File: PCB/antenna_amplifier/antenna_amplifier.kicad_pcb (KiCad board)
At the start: 4 copper layers, 200 x 100 mm, 134 parts, among them J101 PWR_IN 9V, J201 FILT_IN, J202 BIAS, J401 AES3 OUT, J402 S/PDIF OUT, SW301 RESET, SW302 PCM1804 MODE, SW401 CS8406 MODE, U101 ADM7150ARDZ-5.0, U102 ADM7150ARDZ-3.3, U201 LMP7721, U202 LMP7715, U203 LMP7715, U301 LMP7715, U302 PCM1804, U401 CS8406, Y401 24.576MHz, Y402 24.576MHz

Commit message: Amplifier: decouplers next to their supply pins
C206 (U202), C304 (U301), C403 and C404 (U401, CS8406) were 6-8 mm from
the supply pins they decouple; now about 2 mm each. Re-routed; DRC: only
the intended island mask bridges, unconnected 0, parity 0; fit check
clean; fab package refreshed.

Co-Authored-By: Claude Opus 5.5 <noreply@anthropic.com>
Claude-Session: https://claude.ai/code/session_01RsM1DhHhY1tSr2aHjVygSC
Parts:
- moved C304 7.24 mm to (150.2, 64.0), turned to -90 degrees
- moved C404 7.01 mm to (214.4, 101.0), turned to 180 degrees
- moved C206 6.75 mm to (89.6, 115.0), turned to -90 degrees
- moved C403 6.21 mm to (225.6, 100.7), turned to 0 degrees
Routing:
- net /Clock and S/PDIF + AES3 output/APMS: track 80.8 -> 61.0 mm, vias 1 -> 2
- net /Clock and S/PDIF + AES3 output/HWCK1: track 85.8 -> 69.0 mm, vias 1 -> 0
- net /Clock and S/PDIF + AES3 output/CEN: track 62.1 -> 78.6 mm, vias 2 -> 1
- net /Clock and S/PDIF + AES3 output/EMPH_N: track 54.7 -> 70.4 mm, vias 0 -> 1
- net +5VA: track 106.5 -> 97.4 mm, vias 3 -> 4
- net +9V: track 101.0 -> 109.2 mm
- net +3V3: track 191.6 -> 185.0 mm, vias 1 -> 2
- net /ADC (PCM1804)/DRV_OUT: track 55.5 -> 61.3 mm, vias 3 -> 2
- net /Electrometer front end/BIAS_DIV: track 25.1 -> 30.5 mm
- net RESET_N: track 61.4 -> 66.5 mm, vias 3 -> 0
- net /ADC (PCM1804)/VCOML: track 84.3 -> 88.7 mm
- net /Clock and S/PDIF + AES3 output/SFMT1: track 62.9 -> 60.0 mm, vias 0 -> 2
- net /Clock and S/PDIF + AES3 output/HWCK0: track 95.3 -> 92.4 mm
- net GND: track 125.4 -> 127.2 mm, vias 748 -> 756
- net /ADC (PCM1804)/BYPAS: track 30.2 -> 28.4 mm
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
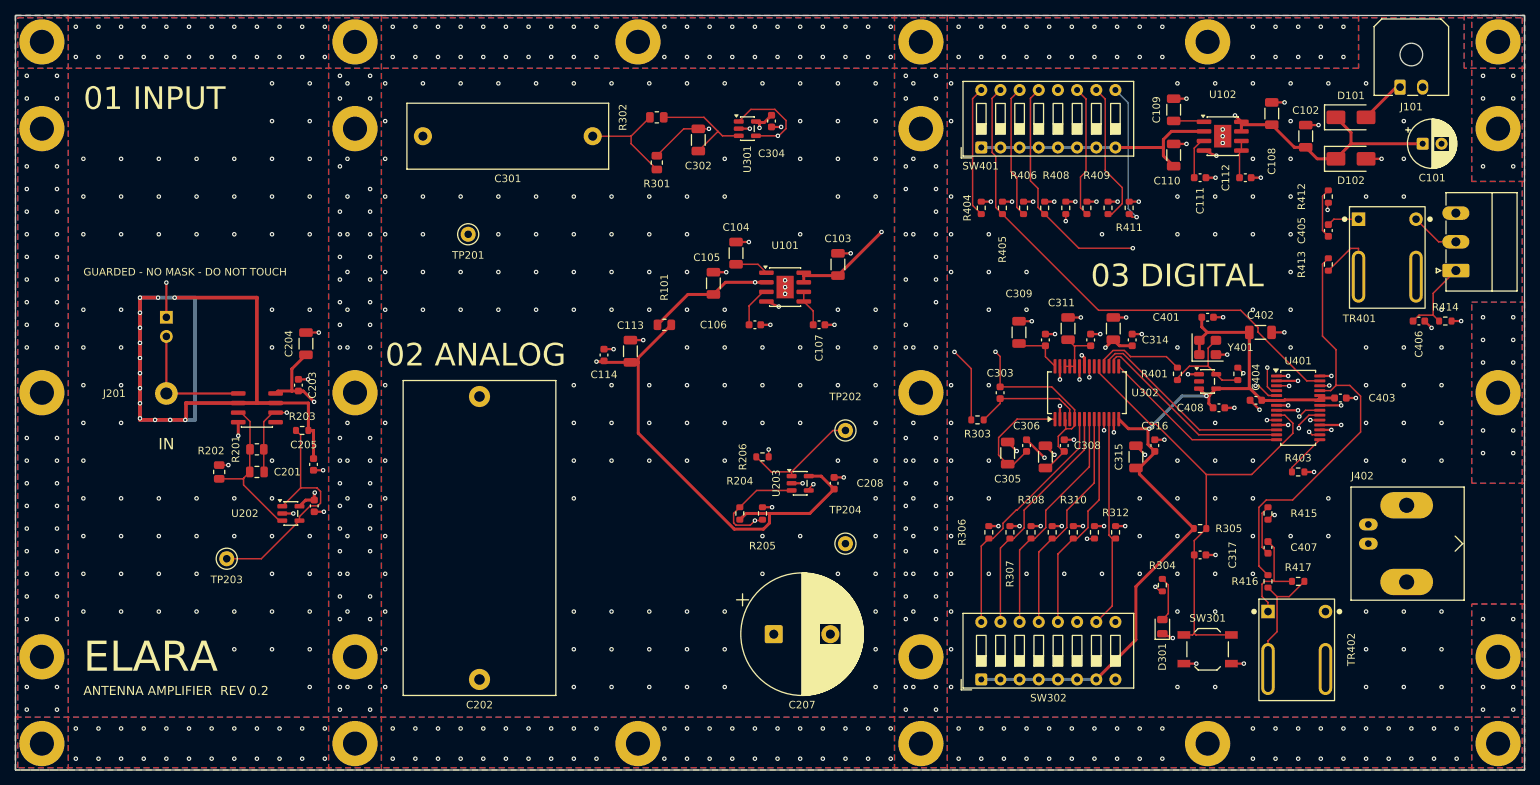
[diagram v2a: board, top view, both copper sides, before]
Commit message: Battery-friendly amplifier, RJ45 AES3 output, tidy placement, 1 mm PSU barrier
Amplifier schematic:
- No LEDs (battery use): the D301 overflow LED becomes test point TP301.
- PCM1804 FMT/S-M/OSR pins use the chip's internal 51 k pull-downs (6 resistors
  gone); BYPAS and the CS8406 mode pins get 47 k: about 3 mA less on +3V3.
- One output: AES3 on a shielded RJ45 (Amphenol RJHSE-5380, blue pair 4/5) for
  shielded twisted-pair cable, transformer isolated; the cable shield floats at
  the receiver (10 nF RF bond DNP, the DC bond is gone). The S/PDIF coax branch
  (BNC, second S22083, 5.6 mA standing current) is removed.

Layout:
- Amplifier re-placed in functional blocks on a 0.5 mm grid: PCM1804 and CS8406
  side by side so the I2S lines run straight, capacitor cells round the LDOs,
  DIP pull-downs in line with the switch pins, guard column in signal order with
  a re-routed hand guard-drive link. RJ45 notch 20 x 16 mm, BNC notch gone.
- PSU tidied (aligned columns, flyback diodes over their relays) and the charger
  / receiver copper kept >= 1.0 mm apart (was 0.30 mm): custom DRC rule, 1 mm
  router class for the relay contacts, hand-routed GND / GND_C at the relays.
- Reference labels follow each part's row; every label on silk except on the
  bare guard island. Fixed two placer bugs: each label counted as its own
  obstacle (SWIG proxies compared with 'is'), and unplaced labels blocked their
  neighbours. Texts are measured by their strokes, not KiCad's text cell.

Mechanics: RJ45 notch, plug envelope and a 1 mm isolation gap in fit_check.
BOM: 502 EUR as designed, 407 EUR recommended; 81 order lines.
Docs: STATUS, PLAN, ASSEMBLY, MOUNTING, README, mechanical and BOM notes;
MAINS_CABLE gains a certified DIY screened-cable option (H07RN-F + foil + braid)
and says why Ethernet cable must not carry mains.

All checks pass (tools/check_all.sh): ERC 0, DRC/parity 0 on all boards (only
the intended guard-island mask bridges), mains clearances, fit check, 27 tests.

Co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
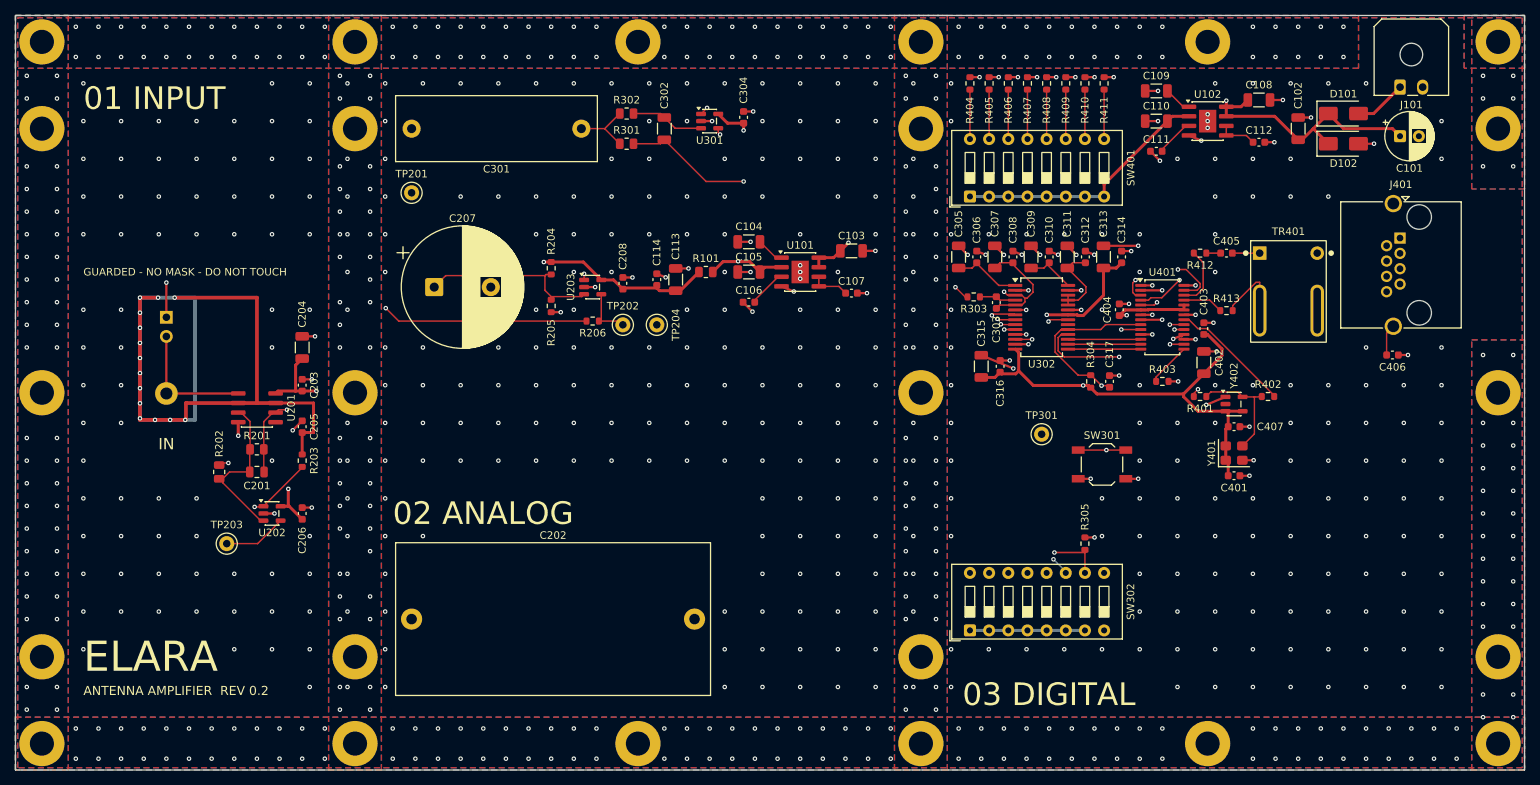
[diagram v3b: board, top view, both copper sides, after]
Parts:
- removed C408: 100n, Capacitor_SMD:C_0603_1608Metric
- removed D301: RED, LED_SMD:LED_0805_2012Metric
- removed J402: S/PDIF OUT, Connector_Coaxial:BNC_Amphenol_B6252HB-NPP3G-50_Horizontal
- removed R306, R307, R308, R309, R310, R311, R312: 10k, Resistor_SMD:R_0603_1608Metric
- removed R414: 0, Resistor_SMD:R_0603_1608Metric
- removed R415, R416: 249, Resistor_SMD:R_0603_1608Metric
- removed R417: 90.9, Resistor_SMD:R_0603_1608Metric
- removed TR402: S22083, elara:Transformer_Pulse_4Pin_W7.62mm
- added TP301: OVFL, TestPoint:TestPoint_Keystone_5000-5004_Miniature, F.Cu at (186.0, 105.5)
- J401: footprint Connector_Phoenix_MC:PhoenixContact_MC_1,5_3-G-3.81_1x03_P3.81mm_Horizontal -> Connector_RJ:RJ45_Amphenol_RJHSE5380
- R304: value 1k -> 10k
- R305, R403, R404, R405, R406, R407, R408, R409, R410, R411: value 10k -> 47k
- moved C207 64.4 mm to (105.5, 86.0)
- moved R204 41.0 mm to (121.0, 83.5), turned to -90 degrees
- moved R205 39.2 mm to (121.0, 88.5), turned to -90 degrees
- moved C208 38.6 mm to (130.5, 85.5)
- moved TP204 38.3 mm to (135.0, 91.0)
- moved U203 37.8 mm to (126.5, 86.0)
- moved TP202 32.7 mm to (130.5, 91.0)
- moved R206 28.8 mm to (126.5, 90.5), turned to 180 degrees
- moved R304 28.6 mm to (192.5, 98.5)
- moved SW301 28.2 mm to (194.0, 109.5)
- moved C307 27.3 mm to (179.8, 82.0)
- moved C305 26.8 mm to (175.0, 82.0)
- moved C317 25.9 mm to (195.0, 98.5), turned to 90 degrees
- moved C308 25.9 mm to (182.2, 82.0)
- moved C306 25.9 mm to (177.4, 82.0)
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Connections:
- net /Clock and S/PDIF + AES3 output/AES_A renamed /Clock and AES3 output/AES_A
- net /Clock and S/PDIF + AES3 output/AES_P1 renamed /Clock and AES3 output/AES_P1
- net /Clock and S/PDIF + AES3 output/AES_P2 renamed /Clock and AES3 output/AES_P2
- net /Clock and S/PDIF + AES3 output/APMS renamed /Clock and AES3 output/APMS
- net /Clock and S/PDIF + AES3 output/AUDIO_N renamed /Clock and AES3 output/AUDIO_N
- net /Clock and S/PDIF + AES3 output/CEN renamed /Clock and AES3 output/CEN
- net /Clock and S/PDIF + AES3 output/EMPH_N renamed /Clock and AES3 output/EMPH_N
- net /Clock and S/PDIF + AES3 output/HWCK0 renamed /Clock and AES3 output/HWCK0
- net /Clock and S/PDIF + AES3 output/HWCK1 renamed /Clock and AES3 output/HWCK1
- net /Clock and S/PDIF + AES3 output/MCLK_TX renamed /Clock and AES3 output/MCLK_TX
- net /Clock and S/PDIF + AES3 output/OSC_OUT renamed /Clock and AES3 output/OSC_OUT
- net /Clock and S/PDIF + AES3 output/SFMT0 renamed /Clock and AES3 output/SFMT0
- net /Clock and S/PDIF + AES3 output/SFMT1 renamed /Clock and AES3 output/SFMT1
- net /Clock and S/PDIF + AES3 output/TCBL renamed /Clock and AES3 output/TCBL
- net /Clock and S/PDIF + AES3 output/TXN renamed /Clock and AES3 output/TXN
- net /Clock and S/PDIF + AES3 output/TXP renamed /Clock and AES3 output/TXP
- C406 pad 1: /Clock and S/PDIF + AES3 output/AES_SHIELD -> /Clock and AES3 output/AES_SHIELD
- C407 pad 1: /Clock and S/PDIF + AES3 output/COAX_A -> +3V3
- C407 pad 2: /Clock and S/PDIF + AES3 output/COAX_P1 -> GND
- J401 pad 1: /Clock and S/PDIF + AES3 output/AES_SHIELD -> unconnected-(J401-Pad1)
- J401 pad 2: /Clock and S/PDIF + AES3 output/AES_HOT -> unconnected-(J401-Pad2)
- J401 pad 3: /Clock and S/PDIF + AES3 output/AES_COLD -> unconnected-(J401-Pad3)
- R304 pad 1: /ADC (PCM1804)/OVFL -> +3V3
- R304 pad 2: /ADC (PCM1804)/LED_OVF -> RESET_N
- R305 pad 1: +3V3 -> /ADC (PCM1804)/BYPAS
- R305 pad 2: RESET_N -> GND
- TR401 pad 3: /Clock and S/PDIF + AES3 output/AES_HOT -> /Clock and AES3 output/AES_HOT
- TR401 pad 4: /Clock and S/PDIF + AES3 output/AES_COLD -> /Clock and AES3 output/AES_COLD
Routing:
- net /Clock and AES3 output/TXN: track 56.1 -> 5.39 mm
- net /Electrometer front end/ANT_BIAS: track 111.9 -> 62.4 mm
- net /Clock and AES3 output/EMPH_N: track 70.4 -> 31.0 mm
- net +5V_PRE: track 131.1 -> 92.1 mm
- net /Clock and AES3 output/TXP: track 47.0 -> 8.11 mm, vias 3 -> 0
- net /Clock and AES3 output/HWCK0: track 92.4 -> 55.0 mm
- net /Clock and AES3 output/CEN: track 78.6 -> 41.3 mm
- net /Clock and S/PDIF + AES3 output/SPDIF_RET: track 34.5 -> 0.00 mm
- net RESET_N: track 66.5 -> 38.4 mm, vias 0 -> 2
- net /Clock and AES3 output/AES_SHIELD: track 0.00 -> 28.1 mm
- net /Clock and AES3 output/SFMT0: track 78.3 -> 51.8 mm
- net /Clock and AES3 output/APMS: track 61.0 -> 38.5 mm, vias 2 -> 1
- net /Clock and AES3 output/AES_COLD: track 0.00 -> 20.4 mm
- net /Clock and AES3 output/AUDIO_N: track 56.9 -> 36.9 mm, vias 2 -> 1
- net LRCK: track 27.6 -> 9.64 mm
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
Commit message: AES3 source resistors 22 ohm for a 111 ohm source; tidy schematics and assembly drawings
- R412/R413 2 x 39 -> 2 x 22 ohm (Vishay TNPW060322R0BEEA, anti-sulfur): the
  CS8406 drivers are 33.5 ohm each at VL = 3.3 V, so 2 x 39 gave a 145 ohm
  source, outside AES3's 110 ohm +-20 %. The schematic note had used the 5 V
  figure and mis-added it.
- AES3 sheet: transformer flipped (kicadgen gains mirror='x') and wired straight
  to R412/R413/C405 and the RJ45, no more touching AES_HOT/AES_COLD labels.
- Stale S/PDIF and 9 V wording out of the sheets and BOM: DC input block reads
  6.98-15 V, J101 'DC IN', PSU J2 'DC OUT', reset button and clock branch say
  AES3; the legacy +9V / +9V_OUT net names are explained on the sheets.
- PSU root sheet gets the same power-path / board summary as the amplifier.
- Assembly drawings: fab-layer copies of the references removed wherever the
  silk reference shows (KiCad 9 texts cannot be hidden), so each part is named
  once; J201/J202 (no silk on the guard island) get theirs beside the part.
- BOM totals +0.14 EUR (502.15 ex VAT reference build, 407.22 recommended).

Co-Authored-By: Claude Opus 5.5 <noreply@anthropic.com>
Claude-Session: https://claude.ai/code/session_01RsM1DhHhY1tSr2aHjVygSC
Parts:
- J101: value PWR_IN 9V -> DC IN
- R412, R413: value 39 -> 22

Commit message: LMP7721 pinout corrected: inputs on pins 1/8, OUT on 4, V+ on 6, V- on 3
The project symbol had IN- on pin 3, GND on 4, OUT on 6 and V+ on 8; as
drawn, the board would have shorted the op-amp's output to GND. The
LMP7721 has both inputs at one end (1 = +IN, 8 = -IN), the N/C isolation
pins 2 and 7 (tied to the guard) next to them, V- on 3, OUT on 4 and V+
on 6 (TI datasheet and evaluation-board notes).

The guard ring already suited the real pinout (inputs at the pin 1/8 end,
guard bar under the body joining pins 2 and 7). Re-placed around U201:
Rf, Cf, Rg and the guard buffer in one column north-east of the chip on a
single hand-routed spine from pin 8; the guard drive (R203, C205) enters
the ring at its north-east corner; V+ decoupling beside pin 6; the V- via
under the body, with nothing else routed there, so OUT leaves pin 4
southwards on In2. HWCK1, which Freerouting now walls in, is pre-routed on
its previous path, and 'finish' removes the router's dangling stubs.
DRC/ERC/parity clean, every label on silk except the two on the bare
island, fit check OK.

Co-Authored-By: Claude Opus 5.5 <noreply@anthropic.com>
Claude-Session: https://claude.ai/code/session_01RsM1DhHhY1tSr2aHjVygSC
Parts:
- moved TP203 40.9 mm to (86.5, 80.0)
- moved C206 27.5 mm to (90.4, 88.6)
- moved U202 25.7 mm to (87.5, 90.5)
- moved R203 21.7 mm to (85.4, 87.5), turned to 180 degrees
- moved C205 20.4 mm to (84.2, 84.5), turned to 0 degrees
- moved R202 19.0 mm to (87.6, 94.7), turned to 0 degrees
- moved C201 14.4 mm to (87.4, 97.1)
- moved C204 12.4 mm to (87.6, 106.4), turned to 0 degrees
- moved R201 9.65 mm to (87.4, 99.5)
- moved C203 4.47 mm to (87.2, 103.4), turned to 0 degrees
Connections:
- U201 pad 3: /Electrometer front end/IN_N -> GND
- U201 pad 4: GND -> PREAMP_OUT
- U201 pad 6: PREAMP_OUT -> +5V_PRE
- U201 pad 8: +5V_PRE -> /Electrometer front end/IN_N
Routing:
- net /Electrometer front end/ANT_BIAS: track 62.4 -> 83.2 mm
- net /Clock and AES3 output/SFMT0: track 51.8 -> 39.5 mm, vias 1 -> 2
- net +5V_PRE: track 92.1 -> 81.5 mm, vias 3 -> 2
- net +3V3: track 195.1 -> 185.0 mm, vias 2 -> 5
- net /Electrometer front end/GUARD_DRV: track 23.4 -> 15.5 mm, vias 1 -> 2
- net /Electrometer front end/GUARD: track 124.0 -> 116.2 mm
- net /Electrometer front end/IN_N: track 21.2 -> 14.2 mm
- net /Electrometer front end/CG: track 34.2 -> 41.1 mm
- net PREAMP_OUT: track 54.8 -> 59.4 mm, vias 1 -> 2
- net /Clock and AES3 output/SFMT1: track 44.3 -> 40.6 mm
- net /Clock and AES3 output/EMPH_N: track 31.0 -> 34.3 mm
- net MCLK_ADC: track 25.1 -> 23.7 mm, vias 2 -> 0
- net GND: track 120.2 -> 119.3 mm
- net /ADC (PCM1804)/DRV_OUT: track 50.0 -> 51.0 mm
- net RESET_N: track 38.4 -> 37.9 mm, vias 2 -> 0
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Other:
- board text added: "DO NOT TOUCH"
- board text added: "GUARDED - NO MASK"
- board text removed: "GUARDED - NO MASK - DO NOT TOUCH"
